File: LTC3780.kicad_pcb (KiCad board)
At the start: 2 copper layers, 100 x 60 mm, 60 parts, among them J1 Screw_Terminal_01x02, J2 Screw_Terminal_01x02, Q2 IPD100N04S402ATMA1, Q3 IPD100N04S402ATMA1, Q4 IPD100N04S402ATMA1, Q5 IPD100N04S402ATMA1, U1 LTC3780EGPBF

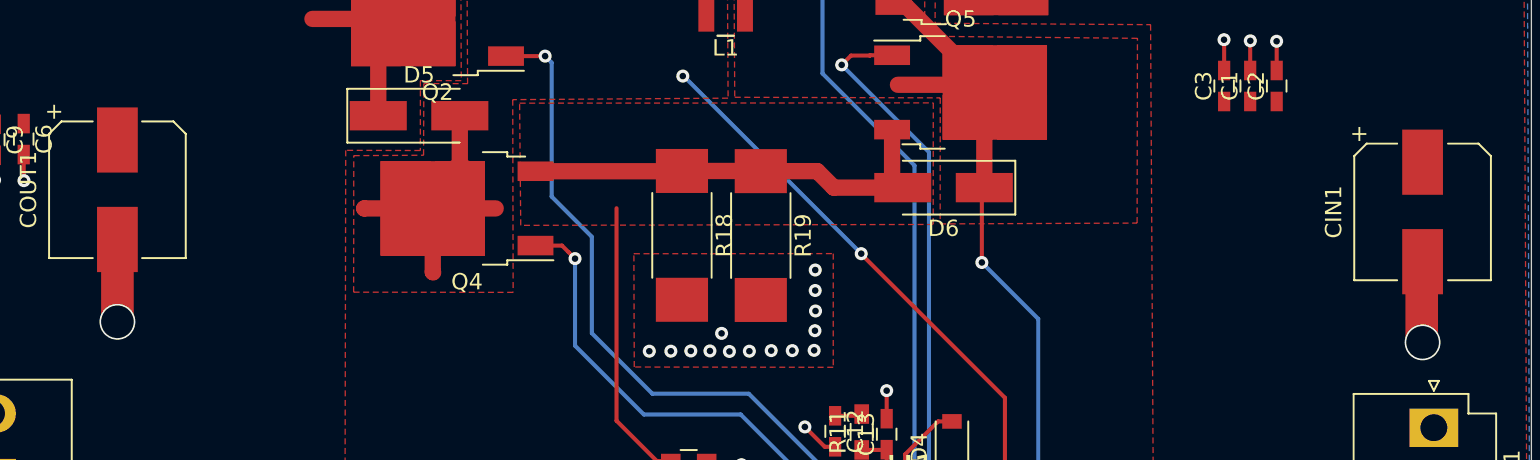
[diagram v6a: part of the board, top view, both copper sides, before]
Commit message: Added additional Capacitor, corrected drill sizes
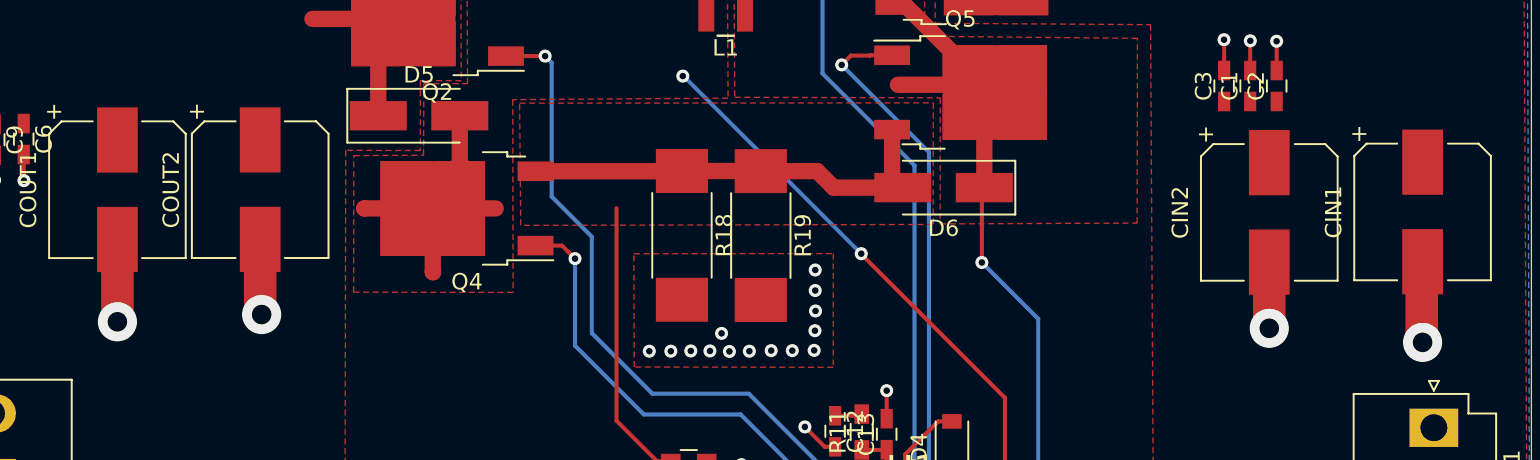
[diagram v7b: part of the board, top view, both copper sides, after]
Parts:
- added CIN2: 22uF, Capacitors_SMD:CP_Elec_8x6.7, F.Cu at (201.9, 71.0)
- added COUT2: 330uF, Capacitors_SMD:CP_Elec_8x10.5, F.Cu at (140.0, 69.6)
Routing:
- net GND: track 49.7 -> 58.4 mm, vias 40 -> 42
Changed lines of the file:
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@@
     (thickness 1.6)
     (drawings 6)
-    (tracks 343)
+    (tracks 348)
     (zones 0)
-    (modules 60)
+    (modules 62)
     (nets 34)
   )
@@
     (pad 1 np_thru_hole circle (at 0 0) (size 4 4) (drill 4) (layers *.Cu *.Mask))
   )
+  (module Capacitors_SMD:CP_Elec_8x6.7 (layer F.Cu)
+    (at 201.92746 71.03672 270)
+    (descr "SMT capacitor, aluminium electrolytic, 8x6.7")
+    (attr smd)
+    (fp_text reference CIN2 (at 0 5.45 270) (layer F.SilkS)
+      (effects (font (size 1 1) (thickness 0.15)))
+    )
+    (fp_text value 22uF (at 0 -5.45 270) (layer F.Fab)
+      (effects (font (size 1 1) (thickness 0.15)))
+    )
+    (fp_line (start 5.3 4.29) (end -5.3 4.29) (layer F.CrtYd) (width 0.05))
+    (fp_line (start 5.3 4.29) (end 5.3 -4.29) (layer F.CrtYd) (width 0.05))
+    (fp_line (start -5.3 -4.29) (end -5.3 4.29) (layer F.CrtYd) (width 0.05))
+    (fp_line (start -5.3 -4.29) (end 5.3 -4.29) (layer F.CrtYd) (width 0.05))
+    (fp_line (start -3.43 -4.19) (end 4.19 -4.19) (layer F.SilkS) (width 0.12))
+    (fp_line (start -4.19 -3.43) (end -3.43 -4.19) (layer F.SilkS) (width 0.12))
+    (fp_line (start -3.43 4.19) (end -4.19 3.43) (layer F.SilkS) (width 0.12))
+    (fp_line (start 4.19 4.19) (end -3.43 4.19) (layer F.SilkS) (width 0.12))
+    (fp_line (start 4.04 -4.04) (end -3.37 -4.04) (layer F.Fab) (width 0.1))
+    (fp_line (start -3.37 -4.04) (end -4.04 -3.37) (layer F.Fab) (width 0.1))
+    (fp_line (start -4.04 -3.37) (end -4.04 3.37) (layer F.Fab) (width 0.1))
+    (fp_line (start -4.04 3.37) (end -3.37 4.04) (layer F.Fab) (width 0.1))
+    (fp_line (start -3.37 4.04) (end 4.04 4.04) (layer F.Fab) (width 0.1))
+    (fp_line (start 4.04 4.04) (end 4.04 -4.04) (layer F.Fab) (width 0.1))
+    (fp_line (start -4.19 3.43) (end -4.19 1.56) (layer F.SilkS) (width 0.12))
+    (fp_line (start -4.19 -3.43) (end -4.19 -1.56) (layer F.SilkS) (width 0.12))
+    (fp_line (start 4.19 -4.19) (end 4.19 -1.56) (layer F.SilkS) (width 0.12))
+    (fp_line (start 4.19 4.19) (end 4.19 1.56) (layer F.SilkS) (width 0.12))
+    (fp_text user %R (at 0 5.45 270) (layer F.Fab)
+      (effects (font (size 1 1) (thickness 0.15)))
+    )
+    (fp_text user + (at -4.78 3.91 270) (layer F.SilkS)
+      (effects (font (size 1 1) (thickness 0.15)))
+    )
+    (fp_text user + (at -1.96 -0.08 270) (layer F.Fab)
+      (effects (font (size 1 1) (thickness 0.15)))
+    )
+    (fp_circle (center 0 0) (end 1 3.8) (layer F.Fab) (width 0.1))
+    (pad 2 smd rect (at 3.05 0 90) (size 4 2.5) (layers F.Cu F.Paste F.Mask)
+      (net 2 GND))
+    (pad 1 smd rect (at -3.05 0 90) (size 4 2.5) (layers F.Cu F.Paste F.Mask)
+      (net 1 +VSW))
+    (model Capacitors_SMD.3dshapes/CP_Elec_8x6.7.wrl
+      (at (xyz 0 0 0))
+      (scale (xyz 1 1 1))
+      (rotate (xyz 0 0 180))
+    )
+  )
+  (module Capacitors_SMD:CP_Elec_8x10.5 (layer F.Cu)
+    (at 140.04798 69.64172 270)
+    (descr "SMT capacitor, aluminium electrolytic, 8x10.5")
+    (attr smd)
+    (fp_text reference COUT2 (at 0 5.45 270) (layer F.SilkS)
+      (effects (font (size 1 1) (thickness 0.15)))
+    )
+    (fp_text value 330uF (at 0 -5.45 270) (layer F.Fab)
+      (effects (font (size 1 1) (thickness 0.15)))
+    )
+    (fp_line (start 5.3 4.29) (end -5.3 4.29) (layer F.CrtYd) (width 0.05))
+    (fp_line (start 5.3 4.29) (end 5.3 -4.29) (layer F.CrtYd) (width 0.05))
+    (fp_line (start -5.3 -4.29) (end -5.3 4.29) (layer F.CrtYd) (width 0.05))
+    (fp_line (start -5.3 -4.29) (end 5.3 -4.29) (layer F.CrtYd) (width 0.05))
+    (fp_line (start -3.43 -4.19) (end 4.19 -4.19) (layer F.SilkS) (width 0.12))
+    (fp_line (start -4.19 -3.43) (end -3.43 -4.19) (layer F.SilkS) (width 0.12))
+    (fp_line (start -3.43 4.19) (end -4.19 3.43) (layer F.SilkS) (width 0.12))
+    (fp_line (start 4.19 4.19) (end -3.43 4.19) (layer F.SilkS) (width 0.12))
+    (fp_line (start 4.19 -4.19) (end 4.19 -1.51) (layer F.SilkS) (width 0.12))
+    (fp_line (start 4.19 4.19) (end 4.19 1.51) (layer F.SilkS) (width 0.12))
+    (fp_line (start -4.19 -3.43) (end -4.19 -1.51) (layer F.SilkS) (width 0.12))
+    (fp_line (start -4.19 3.43) (end -4.19 1.51) (layer F.SilkS) (width 0.12))
+    (fp_line (start 4.04 -4.04) (end -3.37 -4.04) (layer F.Fab) (width 0.1))
+    (fp_line (start -3.37 -4.04) (end -4.04 -3.37) (layer F.Fab) (width 0.1))
+    (fp_line (start -4.04 -3.37) (end -4.04 3.37) (layer F.Fab) (width 0.1))
+    (fp_line (start -4.04 3.37) (end -3.37 4.04) (layer F.Fab) (width 0.1))
+    (fp_line (start -3.37 4.04) (end 4.04 4.04) (layer F.Fab) (width 0.1))
+    (fp_line (start 4.04 4.04) (end 4.04 -4.04) (layer F.Fab) (width 0.1))
+    (fp_text user %R (at 0 5.45 270) (layer F.Fab)
+      (effects (font (size 1 1) (thickness 0.15)))
+    )
+    (fp_text user + (at -4.78 3.91 270) (layer F.SilkS)
+      (effects (font (size 1 1) (thickness 0.15)))
+    )
+    (fp_text user + (at -2.27 -0.08 270) (layer F.Fab)
+      (effects (font (size 1 1) (thickness 0.15)))
+    )
+    (fp_circle (center 0 0) (end 1.3 3.7) (layer F.Fab) (width 0.1))
+    (pad 2 smd rect (at 3.05 0 90) (size 4 2.5) (layers F.Cu F.Paste F.Mask)
+      (net 2 GND))
+    (pad 1 smd rect (at -3.05 0 90) (size 4 2.5) (layers F.Cu F.Paste F.Mask)
+      (net 5 VCC))
+    (model Capacitors_SMD.3dshapes/CP_Elec_8x10.5.wrl
+      (at (xyz 0 0 0))
+      (scale (xyz 1 1 1))
+      (rotate (xyz 0 0 180))
+    )
+  )
   (dimension 99.979481 (width 0.15) (layer Dwgs.User)
     (gr_text "100.00 mm" (at 167.995014 42.41734) (layer Dwgs.User)
@@
   (segment (start 180.56606 102.98176) (end 194.41668 102.98176) (width 0.25) (layer F.Cu) (net 1))
   (segment (start 194.41668 102.98176) (end 194.88912 102.98176) (width 0.25) (layer F.Cu) (net 1))
-  (via (at 211.328 79.0067) (size 2.2) (drill 2) (layers F.Cu B.Cu) (net 2))
+  (via (at 211.328 79.0067) (size 2.4) (drill 1.2) (layers F.Cu B.Cu) (net 2))
   (segment (start 211.27466 79.0829) (end 211.27466 74.55608) (width 2) (layer F.Cu) (net 2) (status 10))
-  (via (at 131.2926 77.74432) (size 2.2) (drill 2) (layers F.Cu B.Cu) (net 2))
+  (via (at 131.2926 77.74432) (size 2.4) (drill 1.2) (layers F.Cu B.Cu) (net 2))
   (segment (start 131.2926 72.6968) (end 131.2926 77.74432) (width 2) (layer F.Cu) (net 2) (status 10))
   (via (at 177.78476 93.11894) (size 0.8) (drill 0.4) (layers F.Cu B.Cu) (net 2))
@@
   (via (at 184.76468 98.19132) (size 0.8) (drill 0.4) (layers F.Cu B.Cu) (net 2))
   (segment (start 183.49472 98.19132) (end 184.76468 98.19132) (width 0.25) (layer F.Cu) (net 2))
+  (via (at 201.92746 78.1431) (size 2.4) (drill 1.2) (layers F.Cu B.Cu) (net 2))
+  (segment (start 201.92746 74.08672) (end 201.92746 78.1431) (width 2) (layer F.Cu) (net 2))
+  (via (at 140.13688 77.29982) (size 2.4) (drill 1.2) (layers F.Cu B.Cu) (net 2))
+  (segment (start 140.04798 77.21092) (end 140.13688 77.29982) (width 2) (layer F.Cu) (net 2))
+  (segment (start 140.04798 72.69172) (end 140.04798 77.21092) (width 2) (layer F.Cu) (net 2))
   (segment (start 187.3098 88.53154) (end 185.71718 86.93892) (width 0.25) (layer F.Cu) (net 4))
   (segment (start 187.3098 89.15654) (end 187.3098 88.53154) (width 0.25) (layer F.Cu) (net 4) (status 10))

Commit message: Updating to latest version tidied routing
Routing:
- net +VSW: track 42.7 -> 47.9 mm
- net SW2: track 63.5 -> 60.4 mm
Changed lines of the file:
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@@
     (thickness 1.6)
     (drawings 6)
-    (tracks 348)
+    (tracks 355)
     (zones 0)
     (modules 62)
@@
   (segment (start 180.56606 102.98176) (end 194.41668 102.98176) (width 0.25) (layer F.Cu) (net 1))
   (segment (start 194.41668 102.98176) (end 194.88912 102.98176) (width 0.25) (layer F.Cu) (net 1))
+  (segment (start 185.17304 56.0451) (end 190.27648 56.0451) (width 1) (layer F.Cu) (net 1))
+  (segment (start 185.17304 52.1451) (end 185.2041 52.11404) (width 1) (layer F.Cu) (net 1))
   (via (at 211.328 79.0067) (size 2.4) (drill 1.2) (layers F.Cu B.Cu) (net 2))
   (segment (start 211.27466 79.0829) (end 211.27466 74.55608) (width 2) (layer F.Cu) (net 2) (status 10))
@@
   (segment (start 184.3024 74.10704) (end 184.3024 69.66712) (width 0.25) (layer F.Cu) (net 21) (status 20))
   (segment (start 184.45226 66.23518) (end 183.42242 65.20534) (width 0.25) (layer F.Cu) (net 21) (status 30))
-  (segment (start 179.44218 58.3251) (end 184.79742 63.68034) (width 0.25) (layer F.Cu) (net 21) (status 30))
   (segment (start 184.79742 63.68034) (end 185.09742 63.68034) (width 0.25) (layer F.Cu) (net 21) (status 30))
   (segment (start 178.87304 58.3251) (end 179.44218 58.3251) (width 0.25) (layer F.Cu) (net 21) (status 30))
   (segment (start 184.45226 64.3255) (end 185.09742 63.68034) (width 2.5) (layer F.Cu) (net 21))
-  (segment (start 179.59218 58.3251) (end 183.42242 62.15534) (width 1) (layer F.Cu) (net 21))
   (segment (start 178.87304 58.3251) (end 179.59218 58.3251) (width 1) (layer F.Cu) (net 21))
   (segment (start 184.45226 63.18518) (end 183.42242 62.15534) (width 1) (layer F.Cu) (net 21))
-  (segment (start 184.45226 69.51726) (end 184.45226 63.18518) (width 1) (layer F.Cu) (net 21))
   (segment (start 184.79742 63.68034) (end 184.32752 63.21044) (width 1) (layer F.Cu) (net 21))
   (segment (start 184.32752 63.21044) (end 179.15636 63.21044) (width 1) (layer F.Cu) (net 21))
+  (segment (start 190.29742 63.68034) (end 190.32028 63.7032) (width 2) (layer F.Cu) (net 21))
+  (segment (start 185.09742 63.68034) (end 190.29742 63.68034) (width 2) (layer F.Cu) (net 21))
+  (segment (start 184.45226 67.54622) (end 184.45226 63.18518) (width 1) (layer F.Cu) (net 21))
+  (segment (start 184.45226 69.51726) (end 184.45226 67.54622) (width 1) (layer F.Cu) (net 21))
+  (segment (start 185.16854 67.5767) (end 184.48274 67.5767) (width 1) (layer F.Cu) (net 21))
+  (segment (start 185.09742 67.50558) (end 185.16854 67.5767) (width 1) (layer F.Cu) (net 21))
+  (segment (start 184.48274 67.5767) (end 184.45226 67.54622) (width 1) (layer F.Cu) (net 21))
+  (segment (start 185.09742 63.68034) (end 185.09742 67.50558) (width 1) (layer F.Cu) (net 21))
   (segment (start 175.641 98.20652) (end 175.54952 98.298) (width 0.25) (layer F.Cu) (net 22) (status 30))
   (segment (start 175.641 96.3676) (end 175.641 98.20652) (width 0.25) (layer F.Cu) (net 22) (status 30))
@@
     (polygon
       (pts
-        (xy 180.80228 47.59452) (xy 169.04716 47.65802) (xy 169.14876 63.97752) (xy 181.7497 64.01308) (xy 181.74462 71.7423)
-        (xy 193.82232 71.6915) (xy 193.84264 60.3631) (xy 180.7972 60.23356)
+        (xy 180.80228 47.59452) (xy 169.04716 47.65802) (xy 169.14876 63.97752) (xy 179.95392 64.008) (xy 181.67604 67.39382)
+        (xy 181.67858 71.75246) (xy 193.82232 71.6915) (xy 193.84264 60.3631) (xy 180.7972 60.23356)
       )
     )
@@
     (polygon
       (pts
-        (xy 118.44274 47.32528) (xy 152.32126 47.67834) (xy 152.37714 62.95898) (xy 149.8727 62.95898) (xy 149.86762 67.24142)
-        (xy 145.29308 67.23126) (xy 145.21434 106.73334) (xy 118.2497 106.7181) (xy 118.1862 67.25158)
+        (xy 118.44274 47.32528) (xy 152.32126 47.67834) (xy 152.37714 62.95898) (xy 149.79142 62.9539) (xy 149.78126 67.0814)
+        (xy 145.29308 67.09156) (xy 145.21434 106.73334) (xy 118.2497 106.7181) (xy 118.1862 67.25158)
       )
     )
@@
     (polygon
       (pts
-        (xy 152.68448 47.67834) (xy 168.64838 47.65802) (xy 168.73982 64.03086) (xy 155.53436 64.1223) (xy 155.55976 75.94092)
-        (xy 145.77822 75.92822) (xy 145.78584 67.55638) (xy 150.06574 67.53098) (xy 150.08352 63.13424) (xy 152.76576 63.14186)
+        (xy 152.70226 47.625) (xy 168.64838 47.625) (xy 168.70426 63.881) (xy 158.79826 63.881) (xy 155.53944 67.35572)
+        (xy 155.55976 75.94092) (xy 145.77822 75.92822) (xy 145.78584 67.55638) (xy 150.0632 67.53352) (xy 150.08352 63.14186)
+        (xy 152.76576 63.1444)
       )
     )
@@
     (polygon
       (pts
-        (xy 155.956 64.3382) (xy 181.32298 64.32042) (xy 181.3179 71.77532) (xy 156.02458 71.8312)
+        (xy 156.0322 67.80022) (xy 159.19196 64.49314) (xy 179.705 64.49568) (xy 180.78704 67.4878) (xy 180.78196 71.77532)
+        (xy 156.02458 71.8312)
       )
     )
